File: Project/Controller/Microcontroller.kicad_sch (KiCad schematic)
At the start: 42 parts, among them J2 SWD, J3 USB_C_Receptacle_USB2.0_16P, SW1 SW_SPDT, SW2 SW_SPDT, SW3 SW_Push, U4 STM32F446RCTx, U5 24AA64-OT, U6 USBLC6-2SC6, Y1 25 MHz

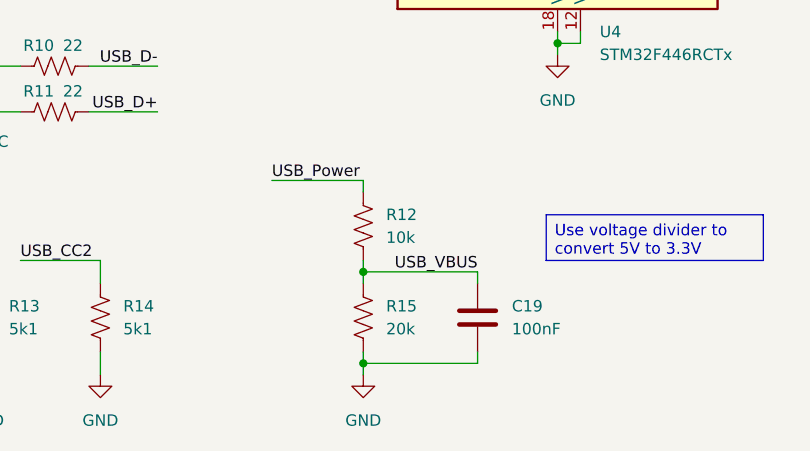
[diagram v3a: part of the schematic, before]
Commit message: Change resistors in VBUS divider
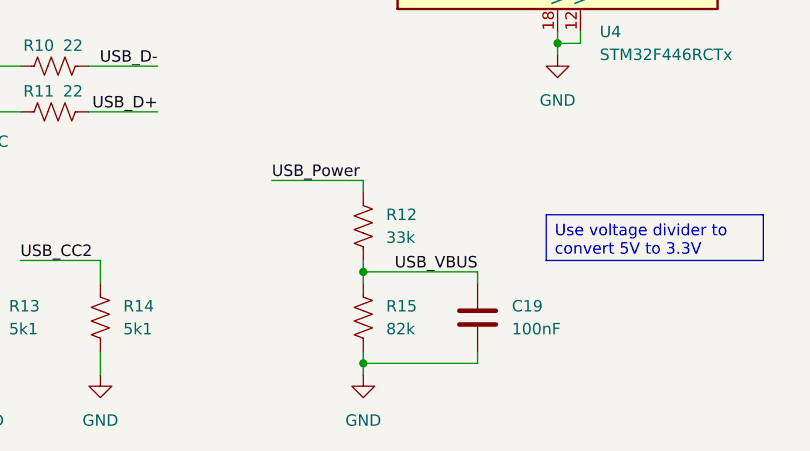
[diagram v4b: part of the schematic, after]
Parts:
- R12: value 10k -> 33k; Listing https://www.digikey.com/en/products/detail/yageo/RC0603FR-0710KL/726880 -> https://www.digikey.com/en/products/detail/yageo/RC0603FR-0733KL/727159
- R15: value 20k -> 82k; Listing https://www.digikey.com/en/products/detail/yageo/RC0603FR-0720KL/727040 -> https://www.digikey.com/en/products/detail/yageo/RC0603FR-0782KL/727400
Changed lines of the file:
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@@
 			)
 		)
-		(property "Value" "10k"
+		(property "Value" "33k"
 			(at 129.54 175.2599 0)
 			(effects
@@
 			)
 		)
-		(property "Datasheet" "https://www.yageogroup.com/content/datasheet/asset/file/PYU-RC_GROUP_51_ROHS_L"
+		(property "Datasheet" "https://yageogroup.com/content/datasheet/asset/file/PYU-RC_GROUP_51_ROHS_L"
 			(at 127 173.99 0)
 			(effects
@@
 			)
 		)
-		(property "Listing" "https://www.digikey.com/en/products/detail/yageo/RC0603FR-0710KL/726880"
+		(property "Listing" "https://www.digikey.com/en/products/detail/yageo/RC0603FR-0733KL/727159"
 			(at 127 173.99 0)
 			(effects
@@
 			)
 		)
-		(property "Value" "20k"
+		(property "Value" "82k"
 			(at 129.54 185.4199 0)
 			(effects
@@
 			)
 		)
-		(property "Datasheet" "https://www.yageogroup.com/content/datasheet/asset/file/PYU-RC_GROUP_51_ROHS_L"
+		(property "Datasheet" "https://yageogroup.com/content/datasheet/asset/file/PYU-RC_GROUP_51_ROHS_L"
 			(at 127 184.15 0)
 			(effects
@@
 			)
 		)
-		(property "Listing" "https://www.digikey.com/en/products/detail/yageo/RC0603FR-0720KL/727040"
+		(property "Listing" "https://www.digikey.com/en/products/detail/yageo/RC0603FR-0782KL/727400"
 			(at 127 184.15 0)
 			(effects

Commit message: Change 0402 footprints to 0603
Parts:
- C10, C11, C12, C14, C15, C19, C31, C8, C9: footprint Capacitor_SMD:C_0402_1005Metric -> Capacitor_SMD:C_0603_1608Metric; Listing https://www.digikey.com/en/products/detail/samsung-electro-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 -> https://www.digikey.com/en/products/detail/yageo/CC0603KRX7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
- C16, C17: footprint Capacitor_SMD:C_0402_1005Metric -> Capacitor_SMD:C_0603_1608Metric; Listing https://www.digikey.com/en/products/detail/yageo/CC0402JRNP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 -> https://www.digikey.com/en/products/detail/kemet/C0603C220J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
- R10, R11, R16, R17, R4, R5, R9: footprint Resistor_SMD:R_0402_1005Metric -> Resistor_SMD:R_0603_1608Metric; Listing https://www.digikey.com/en/products/detail/yageo/RC0402FR-0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 -> https://www.digikey.com/en/products/detail/yageo/RC0603FR-0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
- R6: footprint Resistor_SMD:R_0402_1005Metric -> Resistor_SMD:R_0603_1608Metric; Listing https://www.digikey.com/en/products/detail/stackpole-electronics-inc/RMCF0402FT270R/2417438 -> https://www.digikey.com/en/products/detail/stackpole-electronics-inc/RMCF0603FT270R/1713845
- R7, R8: footprint Resistor_SMD:R_0402_1005Metric -> Resistor_SMD:R_0603_1608Metric; Listing https://www.digikey.com/en/products/detail/yageo/RC0402JR-0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 -> https://www.digikey.com/en/products/detail/yageo/RC0603FR-0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

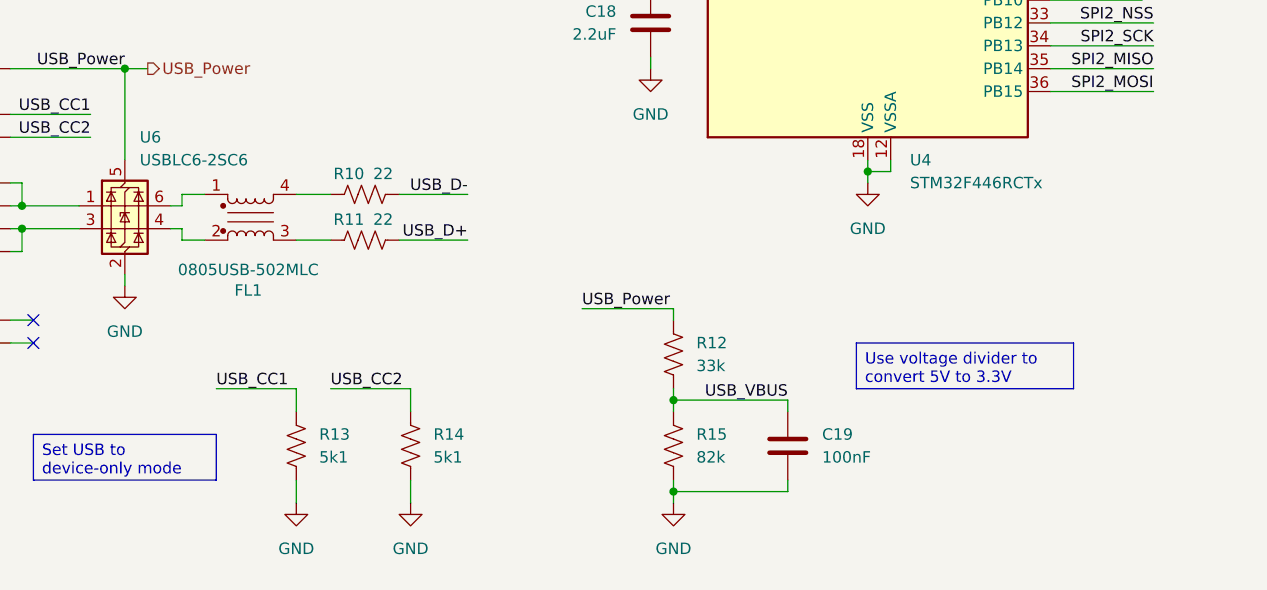
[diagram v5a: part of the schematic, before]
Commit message: Remove redundant USB data line series resistors and CM choke
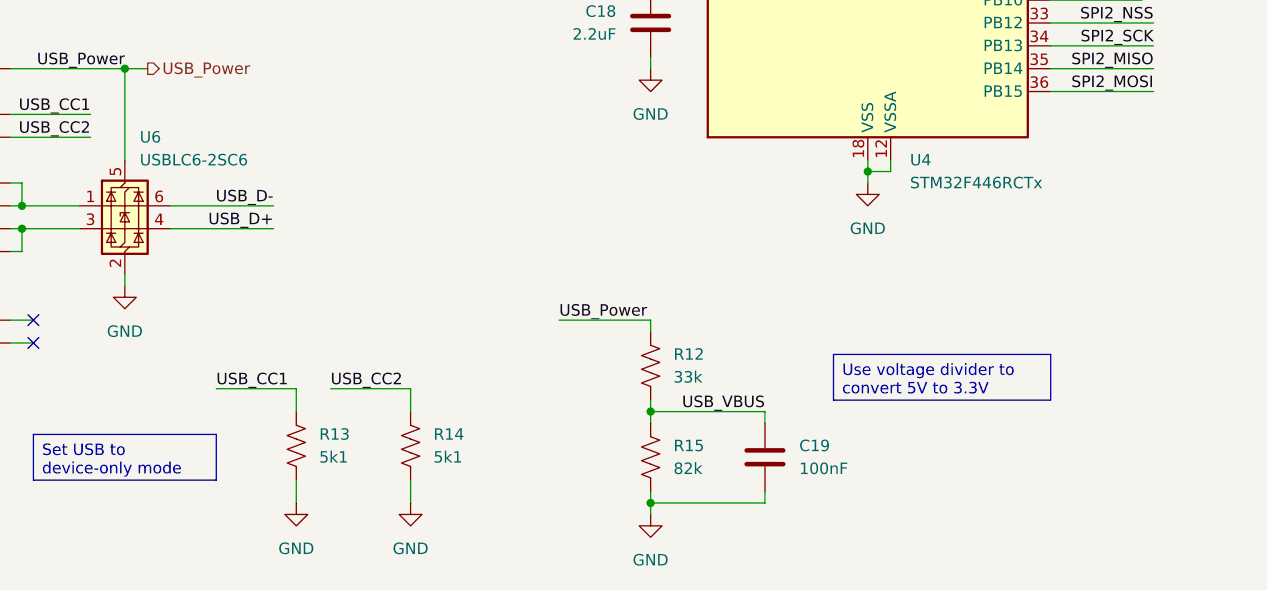
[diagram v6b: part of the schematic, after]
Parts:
- removed FL1: 0805USB-502MLC, Inductor_SMD:L_CommonModeChoke_Coilcraft_0805USB, symbol Device:Filter_EMI_LL_1423
- removed R10, R11: 22, Resistor_SMD:R_0603_1608Metric, symbol Device:R_US
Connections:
- net USB_D+: now also U6.4 (I/O2)
- net USB_D-: now also U6.6 (I/O1)
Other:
- moved on the sheet: C19, R12, R15

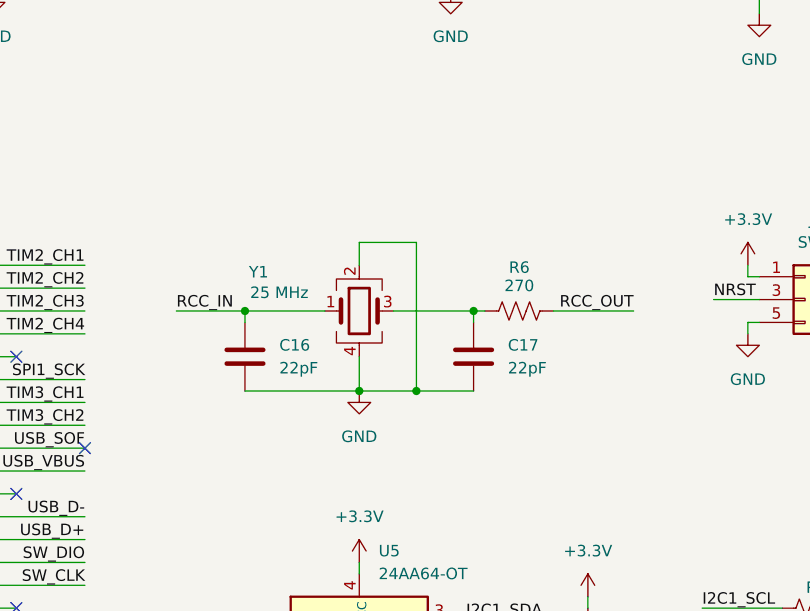
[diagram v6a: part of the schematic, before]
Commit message: Change crystal to 8 MHz
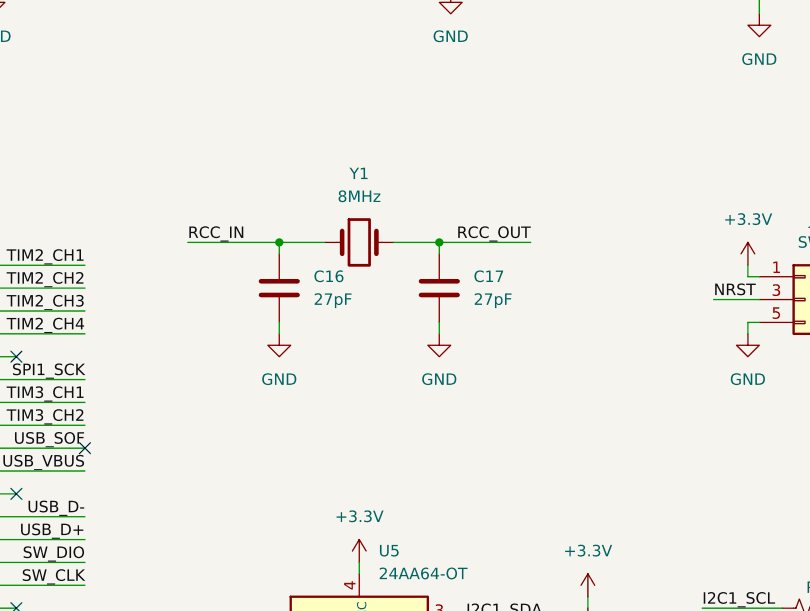
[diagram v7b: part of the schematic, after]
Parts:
- removed R6: 270, Resistor_SMD:R_0603_1608Metric, symbol Device:R_US
- removed Y1: 25 MHz, Crystal:Crystal_SMD_Abracon_ABM8G-4Pin_3.2x2.5mm, symbol Device:Crystal_GND24
- added Y1: 8MHz, Crystal:Crystal_SMD_Abracon_ABM7-2Pin_6.0x3.5mm, symbol Device:Crystal
- C16, C17: value 22pF -> 27pF; Interchangeable Yes -> No; Listing https://www.digikey.com/en/products/detail/kemet/C0603C220J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 -> https://www.digikey.com/en/products/detail/johanson-technol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
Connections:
- net RCC_IN: now also Y1.1
- net RCC_OUT: now also C17.1, Y1.2
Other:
- moved on the sheet: C16, C17

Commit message: Change button to smaller footprint
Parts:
- SW3: footprint Button_Switch_SMD:SW_Push_1P1T_NO_E-Switch_TL3301NxxxxxG -> Button_Switch_SMD:SW_Push_1P1T_NO_CK_KMR2; Listing https://www.digikey.com/en/products/detail/e-switch/TL3301N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 -> https://www.digikey.com/en/products/detail/c-k/KMR211NG-LFS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
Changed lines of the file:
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@@
 			)
 		)
-		(property "Footprint" "Button_Switch_SMD:SW_Push_1P1T_NO_E-Switch_TL3301NxxxxxG"
+		(property "Footprint" "Button_Switch_SMD:SW_Push_1P1T_NO_CK_KMR2"
 			(at 271.78 31.75 0)
 			(effects
@@
 			)
 		)
-		(property "Datasheet" "https://configured-product-images.s3.amazonaws.com/Datasheets/TL3301.pdf"
+		(property "Datasheet" "https://www.ckswitches.com/media/1479/kmr2.pdf"
 			(at 271.78 31.75 0)
 			(effects
@@
 			)
 		)
-		(property "Listing" "https://www.digikey.com/en/products/detail/e-switch/TL3301NF160QG-KR/271564"
+		(property "Listing" "https://www.digikey.com/en/products/detail/c-k/KMR211NG-LFS/2176494"
 			(at 266.7 31.75 90)
 			(effects
